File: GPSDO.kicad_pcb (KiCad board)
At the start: 2 copper layers, 85 x 85 mm, 92 parts, among them J1 Conn_Coaxial, J10 PROG, J2 GPS_CONN, J3 Conn_Coaxial, J4 Conn_Coaxial, J5 Conn_Coaxial, J6 Conn_Coaxial, J7 DISP_MODULE, J8 Barrel_Jack, J9 Conn_Coaxial, SW1 RESET_BTN, U1 REF3450, U10 AZ1117H-5.0TRG1, U11 74AUC1G74, U12 74AUC2G04, U13 74AUC2G04, U14 DS34C87T, U15 MCP6486T-E/OT, U2 74LVC1G125SE-7, U3 AD5680, U4 NB3N551MN, U5 LTC2050IS8, U6 AVR32DB28x-xSO, U7 74LVC1G125SE-7, U8 74HC390, U9 AZ1117H-5.0TRG1, X1 OC5SC25

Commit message: first routing
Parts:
- moved R11 23.2 mm to (30.5, 95.4)
- moved R7 13.2 mm to (32.8, 75.8)
- moved D2 13.2 mm to (30.0, 75.8)
- moved C44 1.40 mm to (28.1, 45.8)
- moved C14 0.85 mm to (40.4, 51.7), turned to 0 degrees
- turned C13 to 0 degrees
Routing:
- net +5VD: track 24.3 -> 323.8 mm, vias 0 -> 15
- net /DAC_MOSI: track 14.1 -> 59.6 mm, vias 0 -> 3
- net +5VA: track 109.8 -> 153.5 mm, vias 1 -> 3
- net /DAC_SCK: track 15.7 -> 57.1 mm, vias 0 -> 4
- net /~{DAC_SS}: track 0.00 -> 34.6 mm, vias 0 -> 3
- net /5Mc_CLK: track 0.00 -> 30.9 mm, vias 0 -> 2
- net GNDA: track 270.5 -> 242.9 mm, vias 6 -> 9
- net /1Mc_CLK: track 0.00 -> 25.6 mm, vias 0 -> 2
- net GND: track 0.00 -> 12.0 mm, vias 6 -> 8
- net Net-(U8-Pad1): track 10.6 -> 11.1 mm
- added copper zone on B.Cu, net GND
- added copper zone on F.Cu, net GND
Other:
- board text added: "TODO: - align connectors to housing and spacing - replace 0R resistors with metal connections - PCB seperators - OXCO footprint - GPS module screw"
- board text removed: "TODO: - align connectors to housing and spacing - replace 0R resistors with metal connections - PCB seperators - OXCO footprint"

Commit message: DRC & ground planes
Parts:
- removed R10, R11: 0R, Resistor_SMD:R_0805_2012Metric_Pad1.20x1.40mm_HandSolder
- added NT1: NetTie_2, Jumper:SolderJumper-2_P1.3mm_Bridged2Bar_RoundedPad1.0x1.5mm, F.Cu at (81.0, 53.7)
- added NT2: NetTie_2, Jumper:SolderJumper-2_P1.3mm_Bridged2Bar_RoundedPad1.0x1.5mm, F.Cu at (28.2, 95.4)
- added TP2: S, TestPoint:TestPoint_THTPad_2.0x2.0mm_Drill1.0mm, F.Cu at (81.0, 57.4)
- added TP3: S, TestPoint:TestPoint_THTPad_2.0x2.0mm_Drill1.0mm, F.Cu at (66.3, 92.5)
- added TP4: S, TestPoint:TestPoint_THTPad_2.0x2.0mm_Drill1.0mm, F.Cu at (103.4, 57.4)
- added TP6: S, TestPoint:TestPoint_THTPad_2.0x2.0mm_Drill1.0mm, F.Cu at (66.3, 57.4)
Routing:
- net GNDA: track 242.9 -> 248.1 mm, vias 9 -> 3
- net GND: track 12.0 -> 9.74 mm, vias 8 -> 6
- net /DAC_SCK: vias 4 -> 3
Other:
- board text added: "Fill with thermal insulation wool"
- board text removed: "Fill space with thermal insulation wool"

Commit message: RC1
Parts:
- added TP2: S, TestPoint:TestPoint_THTPad_2.0x2.0mm_Drill1.0mm, F.Cu at (100.1, 54.9)
- added TP4: S, TestPoint:TestPoint_THTPad_2.0x2.0mm_Drill1.0mm, F.Cu at (63.8, 78.1)
- added TP6: S, TestPoint:TestPoint_THTPad_2.0x2.0mm_Drill1.0mm, F.Cu at (69.5, 54.9)
- added TP8: S, TestPoint:TestPoint_THTPad_2.0x2.0mm_Drill1.0mm, F.Cu at (63.8, 60.8)
- moved C12 1.91 mm to (59.4, 60.8), turned to 0 degrees
- moved J10 0.16 mm to (78.0, 24.6)
- moved J6 0.16 mm to (26.9, 24.6)
- moved J7 0.16 mm to (90.0, 24.6)
- moved J9 0.16 mm to (66.0, 24.6)
- renumbered C7 to C10, C6 to C11, C43 to C12, C42 to C14, C17 to C15, C18 to C16, C16 to C17, C31 to C18, C12 to C19, C5 to C2, C44 to C20, C32 to C21, C19 to C22, C14 to C23, C45 to C24, C15 to C25, C33 to C26, C20 to C27, C34 to C28, C28 to C29, C23 to C3, C35 to C30, C8 to C31, C21 to C32, C22 to C33, C24 to C34, C26 to C35, C29 to C38, C30 to C39, C2 to C4, C41 to C40, C40 to C41, C39 to C42, C38 to C43, C46 to C44, C3 to C5, C25 to C6, C4 to C7, C9 to C8, C27 to C9, J6 to J10, J8 to J2, J10 to J3, J7 to J4, J2 to J5, J9 to J6, J4 to J7, J5 to J8, J3 to J9, R2 to R1, R13 to R10, R12 to R11, R3 to R2, R8 to R3, R9 to R4, R1 to R6, R6 to R8, R4 to R9, TP2 to TP1, TP4 to TP5, TP6 to TP7, U6 to U10, U9 to U11, U10 to U12, U8 to U13, U12 to U2, U13 to U3, U11 to U4, U3 to U5, U4 to U6, U2 to U7, U7 to U8, U5 to U9
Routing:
- net +5VA: track 153.5 -> 154.6 mm
- net +5VD: track 323.8 -> 324.7 mm
- net GND: vias 6 -> 2
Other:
- board text added: "TODO: - PCB seperators - OXCO footprint - GPS module screw"
- board text removed: "TODO: - align connectors to housing and spacing - replace 0R resistors with metal connections - PCB seperators - OXCO footprint - GPS module screw"

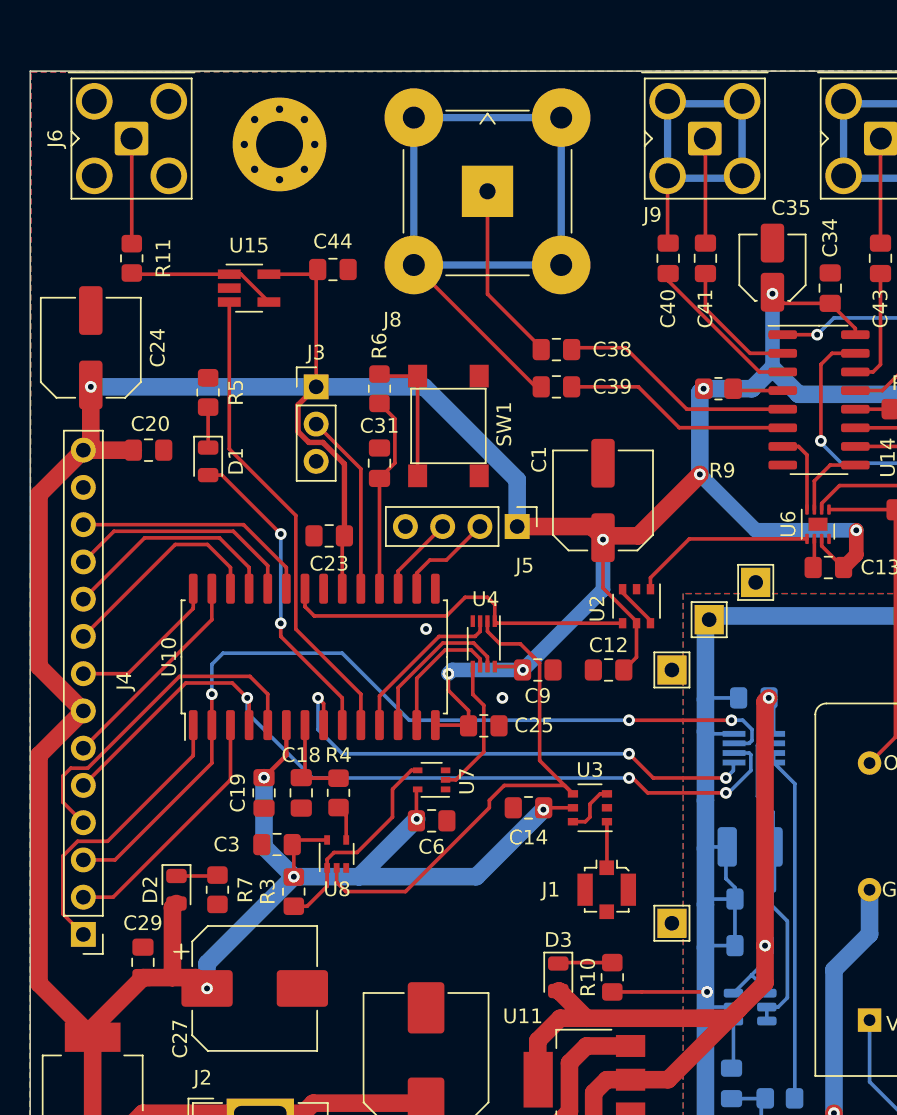
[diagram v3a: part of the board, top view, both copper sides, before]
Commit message: moved components down to accomodate GPS receiver
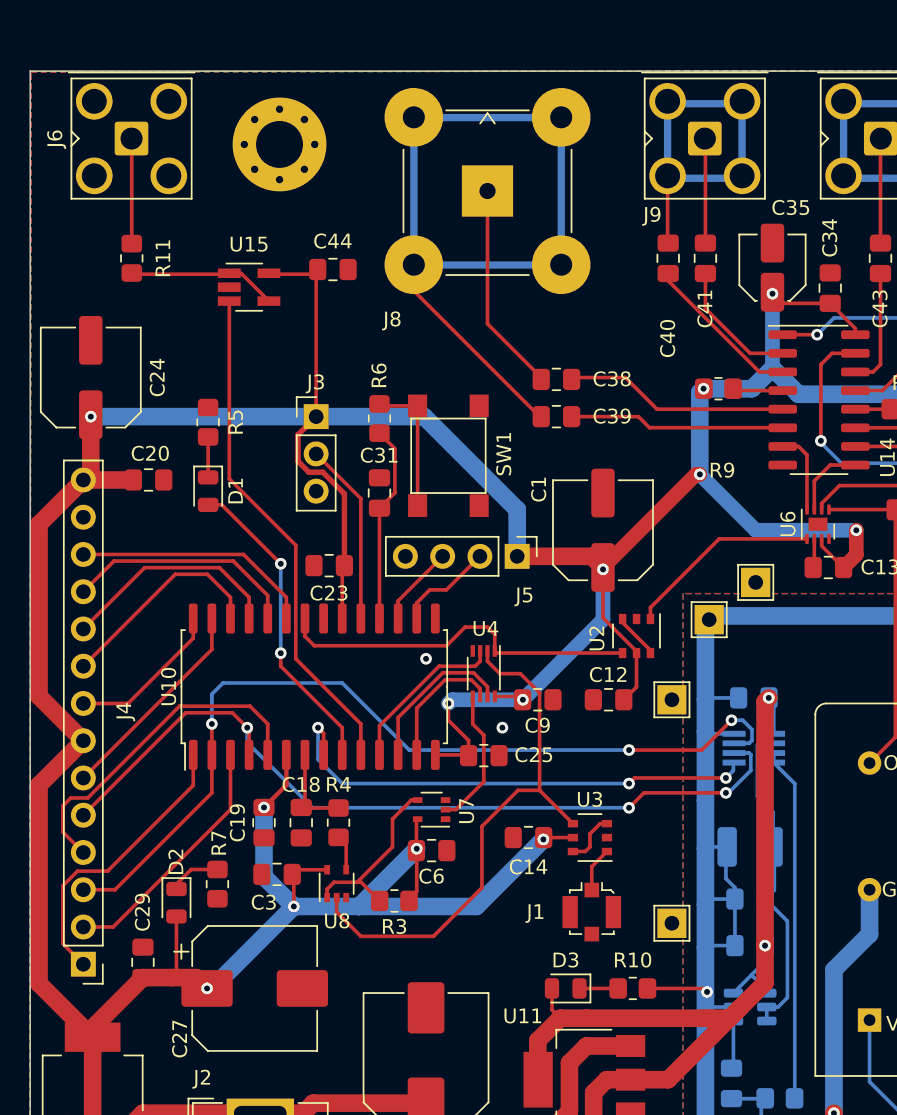
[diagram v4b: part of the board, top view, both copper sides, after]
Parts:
- moved R3 6.89 mm to (44.8, 76.6), turned to 0 degrees
- moved C14 2.03 mm to (54.0, 72.3)
- moved U3 2.03 mm to (58.2, 72.3)
- moved U7 2.03 mm to (47.4, 70.4)
- moved U8 2.03 mm to (40.9, 75.4)
- moved C12 2.03 mm to (59.4, 62.9)
- moved C31 2.03 mm to (43.8, 48.8)
- moved C38 2.03 mm to (55.9, 41.0)
- moved C9 2.03 mm to (54.6, 62.9)
- moved R5 2.03 mm to (32.1, 43.9)
- moved R6 2.03 mm to (43.8, 43.7)
- moved SW1 2.03 mm to (48.5, 46.2)
- moved TP8 2.03 mm to (63.8, 62.9)
- moved U2 2.03 mm to (61.3, 58.5)
- moved U4 2.03 mm to (50.9, 61.1)
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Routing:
- net GNDA: track 248.1 -> 245.8 mm
- net /CUSTOM_OUT: track 32.6 -> 34.7 mm
- net Net-(C38-Pad2): track 12.2 -> 14.2 mm
- net Net-(R3-Pad1): track 14.5 -> 12.5 mm
- net +5VD: track 324.7 -> 326.6 mm
- net Net-(C39-Pad2): track 52.3 -> 54.2 mm
- net /PPS_SIG: track 35.9 -> 37.1 mm
- net Net-(D3-Pad1): track 3.71 -> 2.63 mm
- net Net-(C38-Pad1): track 16.1 -> 15.3 mm
- net Net-(C39-Pad1): track 15.6 -> 14.7 mm
- net /MAIN_CLK_4: track 12.6 -> 13.4 mm
- net /DAC_MOSI: track 59.6 -> 60.4 mm
- net Net-(D2-Pad1): track 2.82 -> 3.54 mm
- net /~{DAC_SS}: track 34.6 -> 34.1 mm

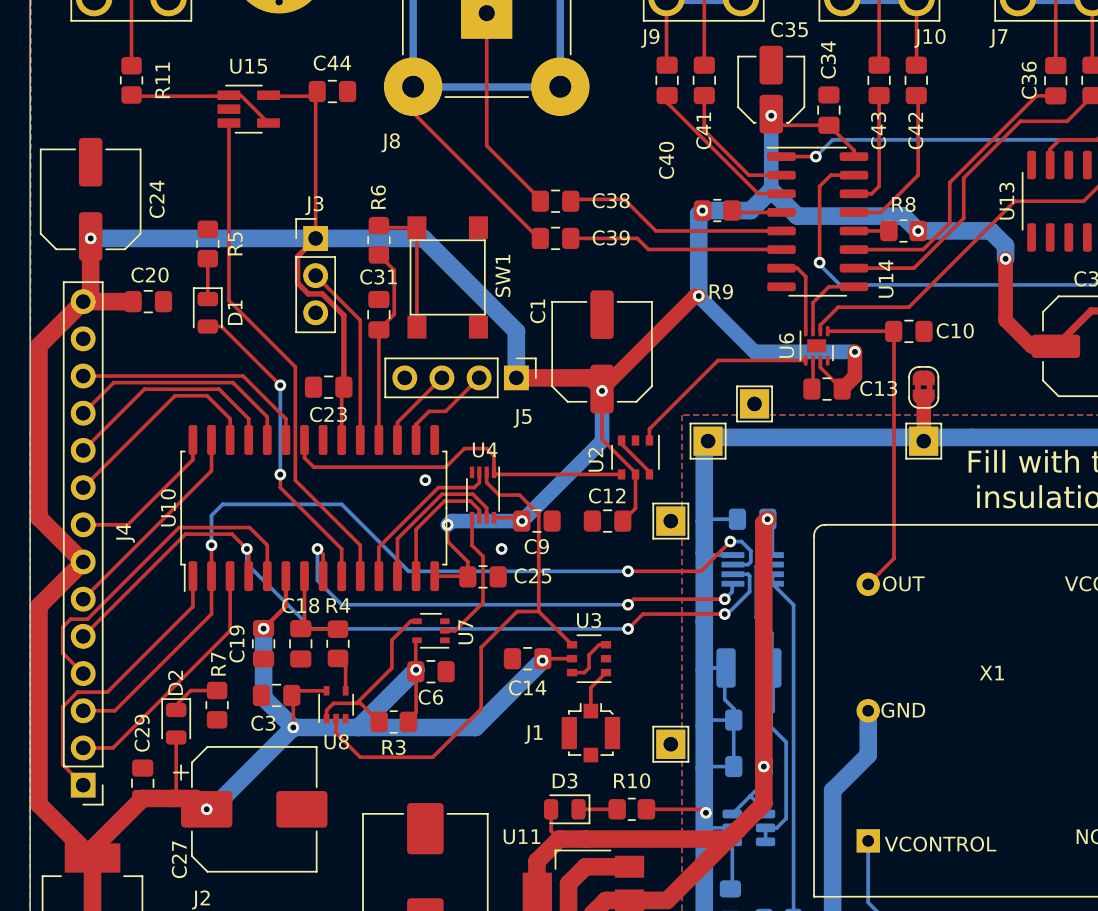
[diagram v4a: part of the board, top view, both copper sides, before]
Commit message: GPS module position
Moved GPS UART connector to 35.1 mm from edge to connect straight to chassis. PCB mounting hole can however not be used.
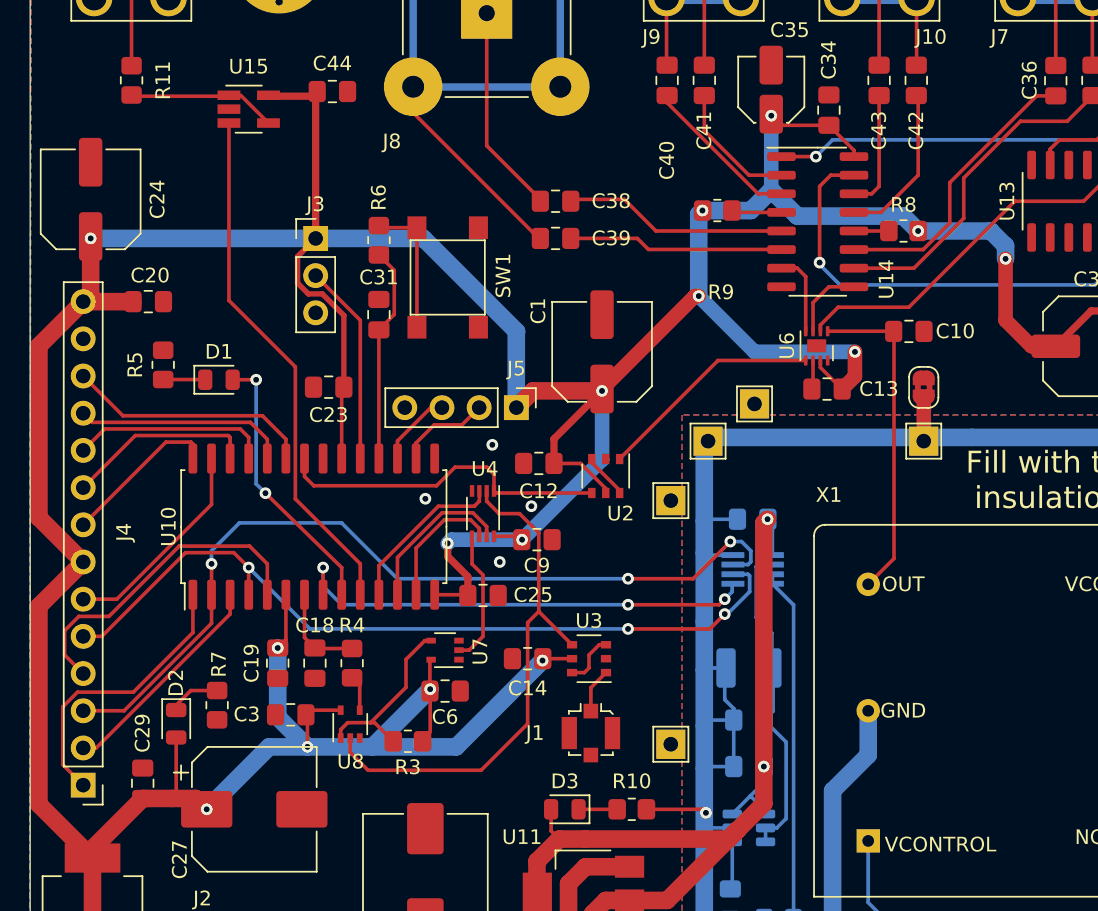
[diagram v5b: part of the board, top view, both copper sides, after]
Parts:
- moved R5 8.80 mm to (29.1, 52.2)
- moved C12 6.13 mm to (54.7, 58.9)
- moved D1 4.64 mm to (32.9, 53.2), turned to 0 degrees
- moved U2 2.40 mm to (59.3, 59.8)
- moved J5 2.03 mm to (53.2, 55.1)
- moved C18 1.64 mm to (39.4, 72.6)
- moved C19 1.64 mm to (36.9, 72.6)
- moved C3 1.64 mm to (37.8, 76.1)
- moved C6 1.64 mm to (48.3, 74.5)
- moved R3 1.64 mm to (45.8, 77.9)
- moved R4 1.64 mm to (42.0, 72.6)
- moved U7 1.64 mm to (48.3, 71.7)
- moved U8 1.64 mm to (41.9, 76.7)
- moved TP8 1.40 mm to (63.8, 61.5)
- moved C9 1.27 mm to (54.6, 64.1)
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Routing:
- net +5VD: track 326.6 -> 331.4 mm
- net Net-(D1-Pad2): track 21.4 -> 18.7 mm
- net /MAIN_CLK_4: track 13.4 -> 15.5 mm
- net /uC_CLK: track 25.1 -> 23.0 mm
- net /TOUCH_MISO: track 17.1 -> 15.1 mm
- net /DAC_SCK: track 57.1 -> 55.3 mm
- net /LCD_MOSI: track 14.7 -> 13.0 mm
- net /LCD_DCRS: track 15.3 -> 13.6 mm
- net /DAC_MOSI: track 60.4 -> 58.7 mm
- net /~{DAC_SS}: track 34.1 -> 32.5 mm
- net /LCD_RESET: track 16.0 -> 14.6 mm
- net /UPDI: track 12.5 -> 13.8 mm
- net /CUSTOM_OUT: track 34.7 -> 35.9 mm
- net /~{RESET}: track 13.5 -> 14.8 mm
- net /~{TOUCH_SS}: track 23.2 -> 22.3 mm
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
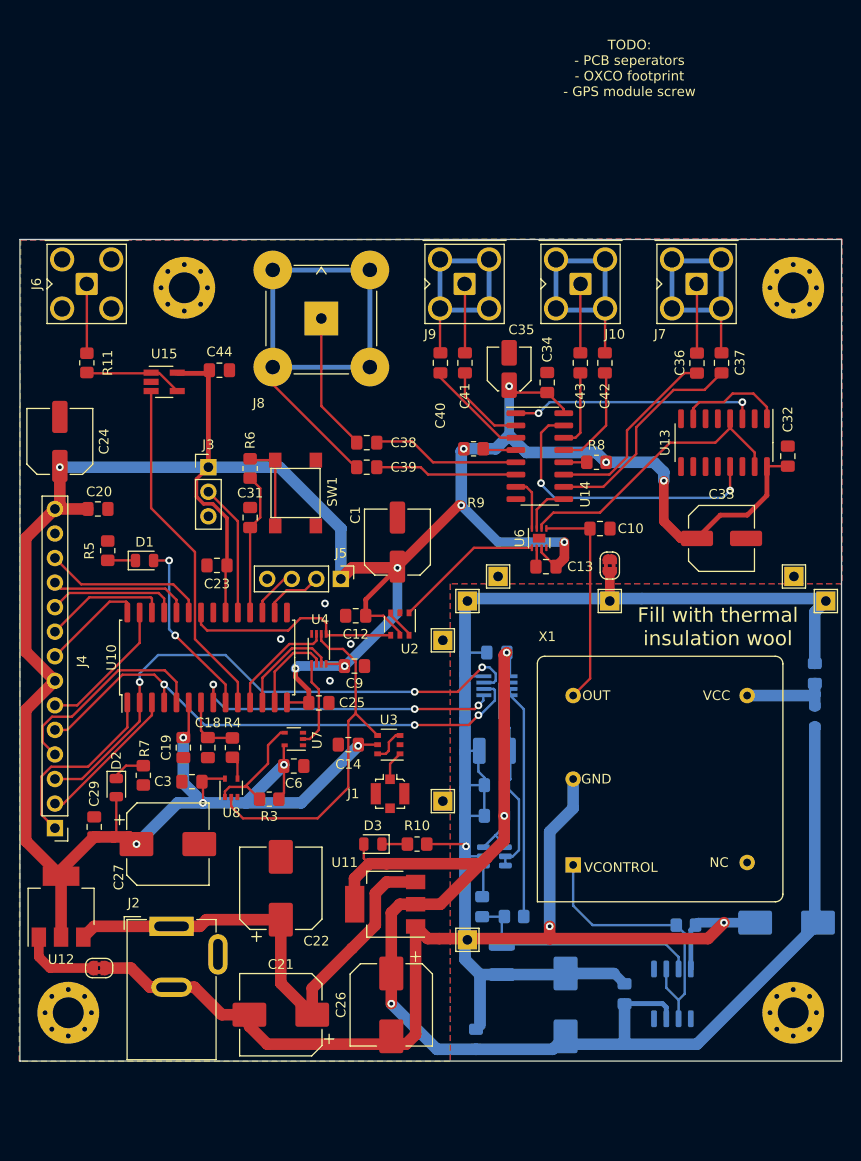
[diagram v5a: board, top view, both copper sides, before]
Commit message: Corrected schematic: VREF
VREF was chosen as 5V instead of 4.096V - corrected with REF3440IDBVR
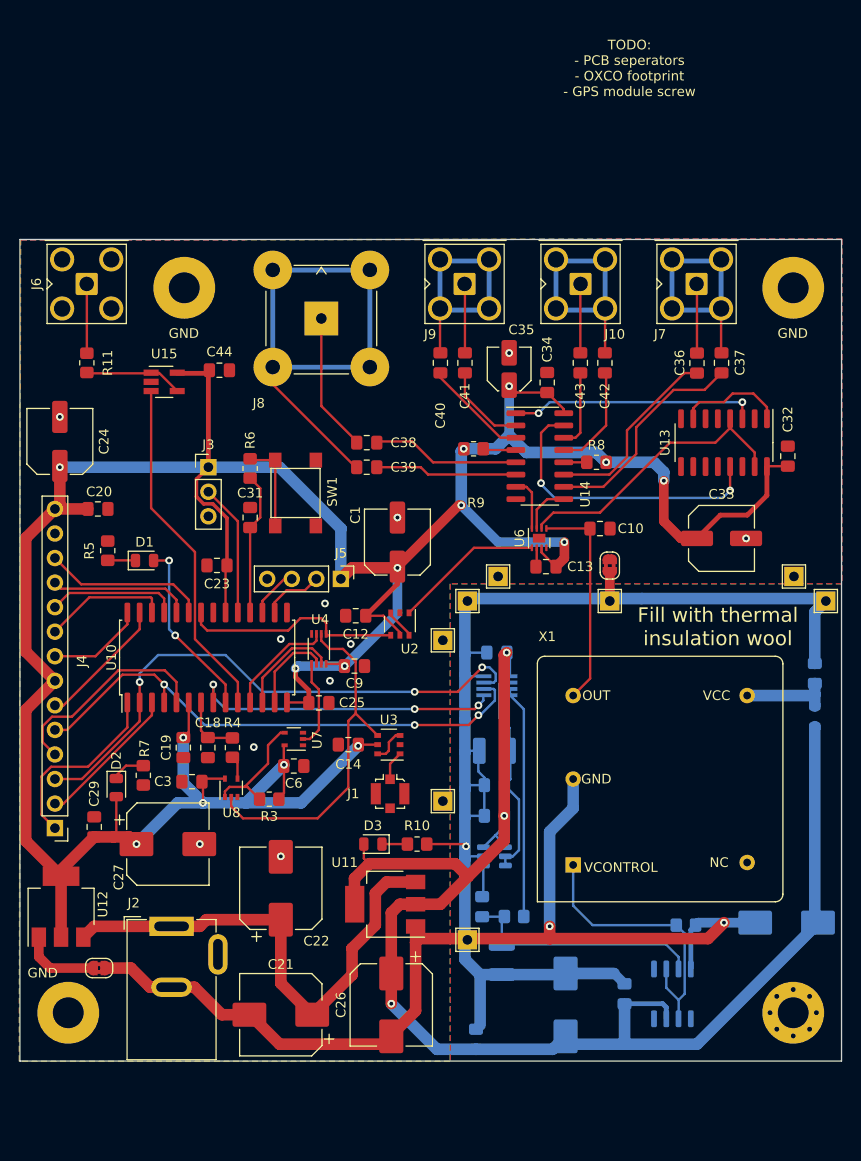
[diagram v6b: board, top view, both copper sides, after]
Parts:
- H1, H2, H3: footprint MountingHole:MountingHole_3.2mm_M3_Pad_Via -> MountingHole:MountingHole_3.2mm_M3_Pad
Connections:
- H1 pad 1: (no net) -> GND
- H2 pad 1: (no net) -> GND
- H3 pad 1: (no net) -> GND
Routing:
- net GNDA: track 245.8 -> 242.8 mm
- net +5VA: track 154.2 -> 152.5 mm
- net /LCD_MISO: track 14.6 -> 13.8 mm
- net /LCD_SCK: track 10.9 -> 10.1 mm
- net GND: vias 4 -> 11
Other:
- board text added: "GND"
